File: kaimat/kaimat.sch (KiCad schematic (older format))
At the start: 4 parts

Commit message: added 2nd encoder
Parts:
- removed SW?: Rotary_Encoder, symbol Device:Rotary_Encoder
- added SW? (x2): Rotary_Encoder_Switch, symbol Device:Rotary_Encoder_Switch
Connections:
- wire segments 19 -> 43
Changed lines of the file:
@@
 EESchema Schematic File Version 4
+LIBS:kaimat-cache
 EELAYER 26 0
 EELAYER END
@@
 F 3 "" H 3300 5350 60  0000 C CNN
 	1    3300 6150
-	1    0    0    -1
-$EndComp
-$Comp
-L Device:Rotary_Encoder SW?
-U 1 1 5C4900BD
-P 2500 3450
-F 0 "SW?" H 2729 3496 50  0000 L CNN
-F 1 "Rotary_Encoder" H 2729 3405 50  0000 L CNN
-F 2 "" H 2350 3610 50  0001 C CNN
-F 3 "~" H 2500 3710 50  0001 C CNN
-	1    2500 3450
 	1    0    0    -1
 $EndComp
@@
 Wire Wire Line
 	1400 6150 2300 6150
+$Comp
+L Device:Rotary_Encoder_Switch SW?
+U 1 1 5C5B4CB3
+P 2600 4200
+F 0 "SW?" H 2600 4567 50  0000 C CNN
+F 1 "Rotary_Encoder_Switch" H 2600 4476 50  0000 C CNN
+F 2 "" H 2450 4360 50  0001 C CNN
+F 3 "~" H 2600 4460 50  0001 C CNN
+	1    2600 4200
+	1    0    0    -1
+$EndComp
 Wire Wire Line
-	650  4850 2300 4850
+	2300 4200 2100 4200
 Wire Wire Line
-	1800 3550 1800 4950
+	2100 4200 2100 4600
 Wire Wire Line
-	1800 4950 2300 4950
+	650  4850 2100 4850
+Connection ~ 2100 4850
 Wire Wire Line
-	1750 3450 1750 5050
+	2100 4850 2300 4850
 Wire Wire Line
-	1750 5050 2300 5050
+	3050 4600 3050 4300
 Wire Wire Line
-	1700 3350 1700 5150
+	3050 4300 2900 4300
 Wire Wire Line
-	1700 5150 2300 5150
+	2100 4600 3050 4600
+Connection ~ 2100 4600
 Wire Wire Line
-	1800 3550 2200 3550
+	2100 4600 2100 4850
 Wire Wire Line
-	1750 3450 2200 3450
+	2900 4100 2950 4100
 Wire Wire Line
-	1700 3350 2200 3350
+	2950 4100 2950 4700
+Wire Wire Line
+	2950 4700 2250 4700
+Wire Wire Line
+	2250 4700 2250 4950
+Wire Wire Line
+	2250 4950 2300 4950
+Wire Wire Line
+	2300 5050 2200 5050
+Wire Wire Line
+	2200 5050 2200 4300
+Wire Wire Line
+	2200 4300 2300 4300
+Wire Wire Line
+	2300 4100 2150 4100
+Wire Wire Line
+	2150 5150 2300 5150
+Wire Wire Line
+	2150 4100 2150 5150
+$Comp
+L Device:Rotary_Encoder_Switch SW?
+U 1 1 5C5B60FE
+P 2600 3500
+F 0 "SW?" H 2600 3867 50  0000 C CNN
+F 1 "Rotary_Encoder_Switch" H 2600 3776 50  0000 C CNN
+F 2 "" H 2450 3660 50  0001 C CNN
+F 3 "~" H 2600 3760 50  0001 C CNN
+	1    2600 3500
+	1    0    0    -1
+$EndComp
+Wire Wire Line
+	2100 4200 2100 3500
+Wire Wire Line
+	2100 3500 2300 3500
+Connection ~ 2100 4200
+Wire Wire Line
+	2900 3600 3050 3600
+Wire Wire Line
+	3050 3600 3050 4300
+Connection ~ 3050 4300
+Wire Wire Line
+	2900 3400 3150 3400
+Wire Wire Line
+	3150 3400 3150 3050
+Wire Wire Line
+	3150 3050 1950 3050
+Wire Wire Line
+	1950 3050 1950 6850
+Wire Wire Line
+	1950 6850 2300 6850
+Wire Wire Line
+	2300 3400 2000 3400
+Wire Wire Line
+	2000 6950 2300 6950
+Wire Wire Line
+	2000 3400 2000 6950
+Wire Wire Line
+	2300 3600 1850 3600
+Wire Wire Line
+	1850 3600 1850 7050
+Wire Wire Line
+	1850 7050 2300 7050
 $EndSCHEMATC

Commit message: added pannel
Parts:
- added D? (x2): DIODE, symbol pspice:DIODE
- added J? (x2): AudioJack2_Ground, symbol Connector:AudioJack2_Ground
- added R? (x4): R, symbol Device:R
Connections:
- new net: J?.G, R?.1 (x2)
- new net: J?.S, R?.2 (x2)
- new net: D?.1 (K), R?.1, R?.2 (x2)
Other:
- note added: "1000"
- note added: "330"
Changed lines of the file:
@@
 	650  3500 800  3500
-Wire Wire Line
-	650  4850 650  4050
-Wire Wire Line
-	650  4050 650  3500
-Connection ~ 650  4050
 Wire Wire Line
 	1400 3500 1550 3500
@@
 Wire Wire Line
 	2100 3500 2300 3500
+Wire Wire Line
+	2900 3600 3050 3600
+Wire Wire Line
+	3050 3600 3050 4300
+Wire Wire Line
+	2900 3400 3150 3400
+Wire Wire Line
+	3150 3400 3150 3050
+Wire Wire Line
+	3150 3050 1950 3050
+Wire Wire Line
+	1950 3050 1950 6850
+Wire Wire Line
+	1950 6850 2300 6850
+Wire Wire Line
+	2300 3400 2000 3400
+Wire Wire Line
+	2000 6950 2300 6950
+Wire Wire Line
+	2000 3400 2000 6950
+Wire Wire Line
+	2300 3600 1850 3600
+Wire Wire Line
+	1850 3600 1850 7050
+Wire Wire Line
+	1850 7050 2300 7050
+$Comp
+L Connector:AudioJack2_Ground J?
+U 1 1 5C5C6F4A
+P 800 900
+F 0 "J?" H 830 1225 50  0000 C CNN
+F 1 "AudioJack2_Ground" H 830 1134 50  0000 C CNN
+F 2 "" H 800 900 50  0001 C CNN
+F 3 "~" H 800 900 50  0001 C CNN
+	1    800  900
+	1    0    0    -1
+$EndComp
+$Comp
+L Device:R R?
+U 1 1 5C5C70ED
+P 1150 1100
+F 0 "R?" H 1220 1146 50  0000 L CNN
+F 1 "R" H 1220 1055 50  0000 L CNN
+F 2 "" V 1080 1100 50  0001 C CNN
+F 3 "~" H 1150 1100 50  0001 C CNN
+	1    1150 1100
+	0    -1   1    0
+$EndComp
+Text Notes 1050 1150 0    50   ~ 0
+330
+$Comp
+L Device:R R?
+U 1 1 5C5C72C2
+P 1150 800
+F 0 "R?" H 1220 846 50  0000 L CNN
+F 1 "R" H 1220 755 50  0000 L CNN
+F 2 "" V 1080 800 50  0001 C CNN
+F 3 "~" H 1150 800 50  0001 C CNN
+	1    1150 800
+	0    1    1    0
+$EndComp
+Wire Wire Line
+	800  1100 1000 1100
+Text Notes 1050 850  0    50   ~ 0
+1000
+Wire Wire Line
+	1300 800  1500 800
+Wire Wire Line
+	1300 1100 1500 1100
+Wire Wire Line
+	1500 1100 1500 800
+Wire Wire Line
+	1500 800  1700 800
+Connection ~ 1500 800
+$Comp
+L Connector:AudioJack2_Ground J?
+U 1 1 5C5D9E79
+P 800 1500
+F 0 "J?" H 830 1825 50  0000 C CNN
+F 1 "AudioJack2_Ground" H 830 1734 50  0000 C CNN
+F 2 "" H 800 1500 50  0001 C CNN
+F 3 "~" H 800 1500 50  0001 C CNN
+	1    800  1500
+	1    0    0    -1
+$EndComp
+$Comp
+L Device:R R?
+U 1 1 5C5D9E80
+P 1150 1700
+F 0 "R?" H 1220 1746 50  0000 L CNN
+F 1 "R" H 1220 1655 50  0000 L CNN
+F 2 "" V 1080 1700 50  0001 C CNN
+F 3 "~" H 1150 1700 50  0001 C CNN
+	1    1150 1700
+	0    -1   1    0
+$EndComp
+Text Notes 1050 1750 0    50   ~ 0
+330
+$Comp
+L Device:R R?
+U 1 1 5C5D9E88
+P 1150 1400
+F 0 "R?" H 1220 1446 50  0000 L CNN
+F 1 "R" H 1220 1355 50  0000 L CNN
+F 2 "" V 1080 1400 50  0001 C CNN
+F 3 "~" H 1150 1400 50  0001 C CNN
+	1    1150 1400
+	0    1    1    0
+$EndComp
+Wire Wire Line
+	800  1700 1000 1700
+Text Notes 1050 1450 0    50   ~ 0
+1000
+Wire Wire Line
+	1300 1400 1500 1400
+Wire Wire Line
+	1300 1700 1500 1700
+Wire Wire Line
+	1500 1700 1500 1400
+Wire Wire Line
+	1500 1400 1700 1400
+Connection ~ 1500 1400
+$Comp
+L pspice:DIODE D?
+U 1 1 5C5DC9CE
+P 1900 800
+F 0 "D?" H 1900 1065 50  0000 C CNN
+F 1 "DIODE" H 1900 974 50  0000 C CNN
+F 2 "" H 1900 800 50  0001 C CNN
+F 3 "~" H 1900 800 50  0001 C CNN
+	1    1900 800
+	1    0    0    -1
+$EndComp
+$Comp
+L pspice:DIODE D?
+U 1 1 5C5DCA79
+P 1900 1400
+F 0 "D?" H 1900 1665 50  0000 C CNN
+F 1 "DIODE" H 1900 1574 50  0000 C CNN
+F 2 "" H 1900 1400 50  0001 C CNN
+F 3 "~" H 1900 1400 50  0001 C CNN
+	1    1900 1400
+	1    0    0    -1
+$EndComp
+Wire Wire Line
+	650  4050 650  3500
+Wire Wire Line
+	650  4850 650  4050
+Connection ~ 650  4050
+Connection ~ 3050 4300
 Connection ~ 2100 4200
-Wire Wire Line
-	2900 3600 3050 3600
-Wire Wire Line
-	3050 3600 3050 4300
-Connection ~ 3050 4300
-Wire Wire Line
-	2900 3400 3150 3400
-Wire Wire Line
-	3150 3400 3150 3050
-Wire Wire Line
-	3150 3050 1950 3050
-Wire Wire Line
-	1950 3050 1950 6850
-Wire Wire Line
-	1950 6850 2300 6850
-Wire Wire Line
-	2300 3400 2000 3400
-Wire Wire Line
-	2000 6950 2300 6950
-Wire Wire Line
-	2000 3400 2000 6950
-Wire Wire Line
-	2300 3600 1850 3600
-Wire Wire Line
-	1850 3600 1850 7050
-Wire Wire Line
-	1850 7050 2300 7050
 $EndSCHEMATC

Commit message: schematic finished
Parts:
- removed U?: Teensy3.2, symbol teensy:Teensy3.2
- added D? (x2): DIODE, symbol pspice:DIODE
- added J? (x2): AudioJack2_Ground, symbol Connector:AudioJack2_Ground
- added R? (x4): R, symbol Device:R
- added U?: Teensy3.6, symbol teensy:Teensy3.6
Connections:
- net labels added: 3.3V, 3.3v, DACclr, DACdataout, DACldac, DACslaveSelect, DACspiclk, GND, OLEDclock, OLEDcs, OLEDdata, OLEDdc, OLEDreset, b1, b2, cvIn1, cvIn2, cvIn3, cvIn4, enc1button, enc1pinA, enc1pinB, enc2button, enc2pinA, enc2pinB, trellisSCL, trellisSDA
- wire segments 53 -> 59
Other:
- note added: "Adafruit NeoTrellis"
- note added: "TI DAC8568ICPW"
- note added: "WaveShare 128x128 OLED"
- moved on the sheet: D?, J?, R?, SW?

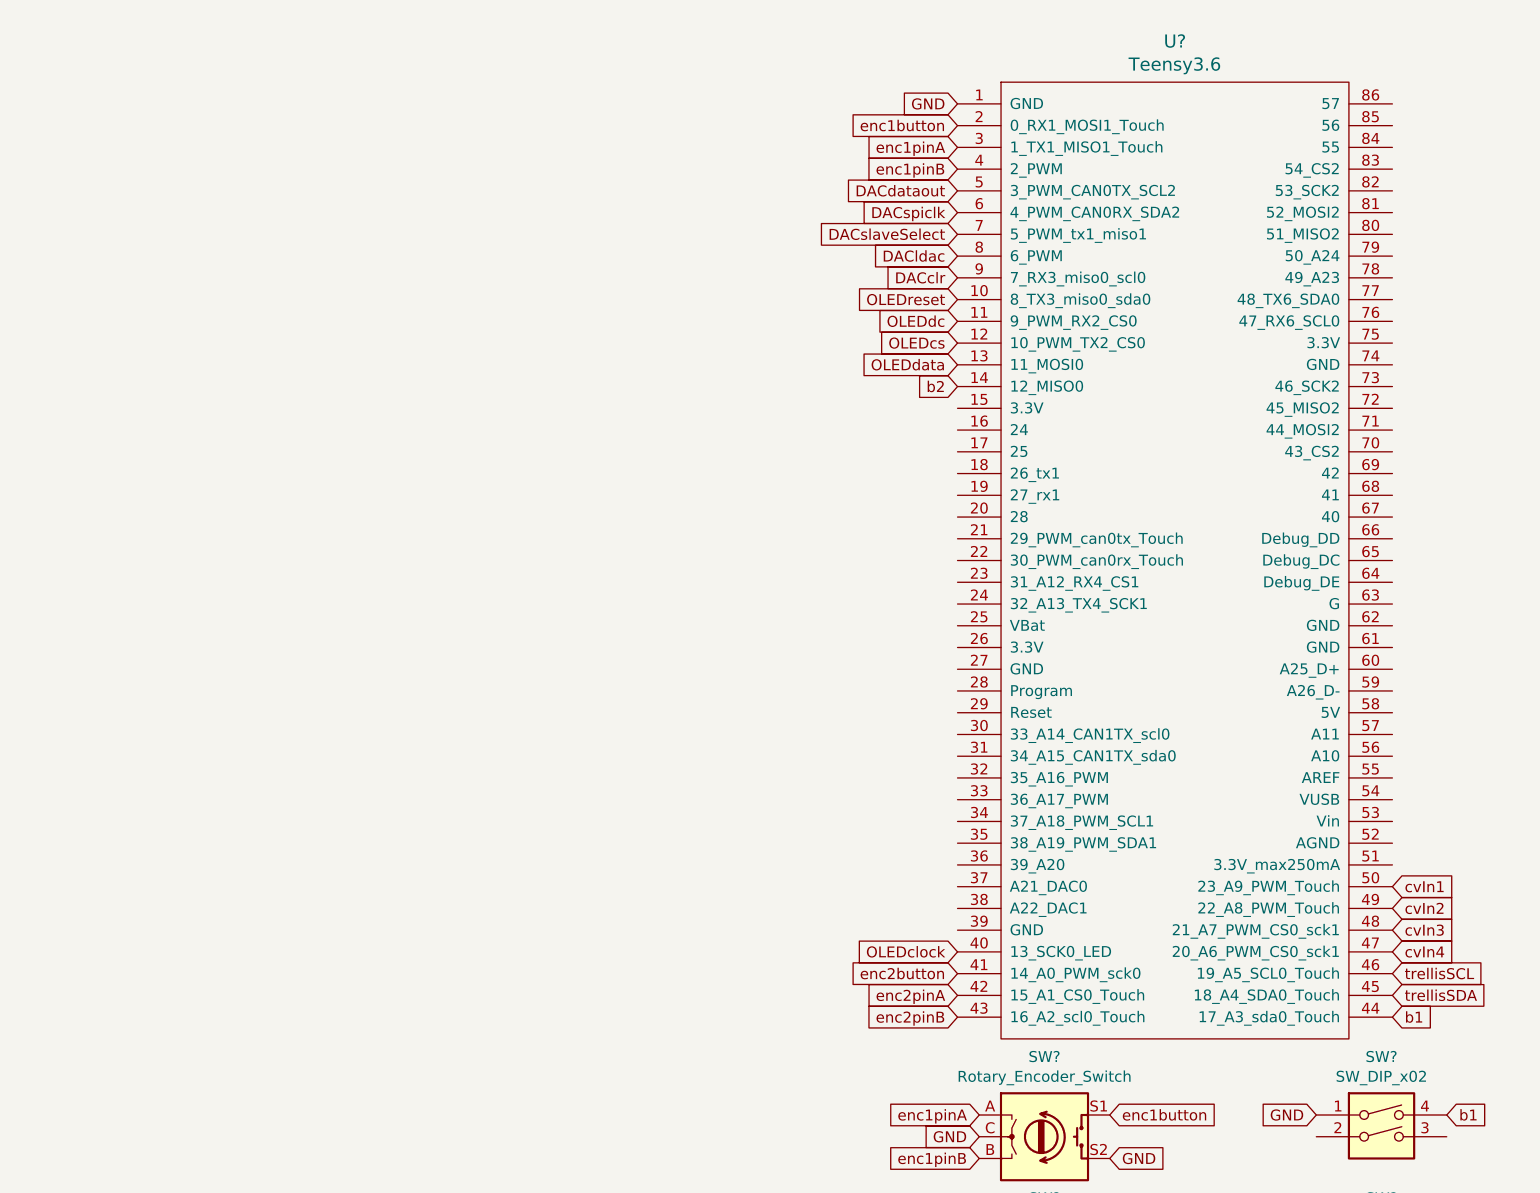
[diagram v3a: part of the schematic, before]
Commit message: schematic improved
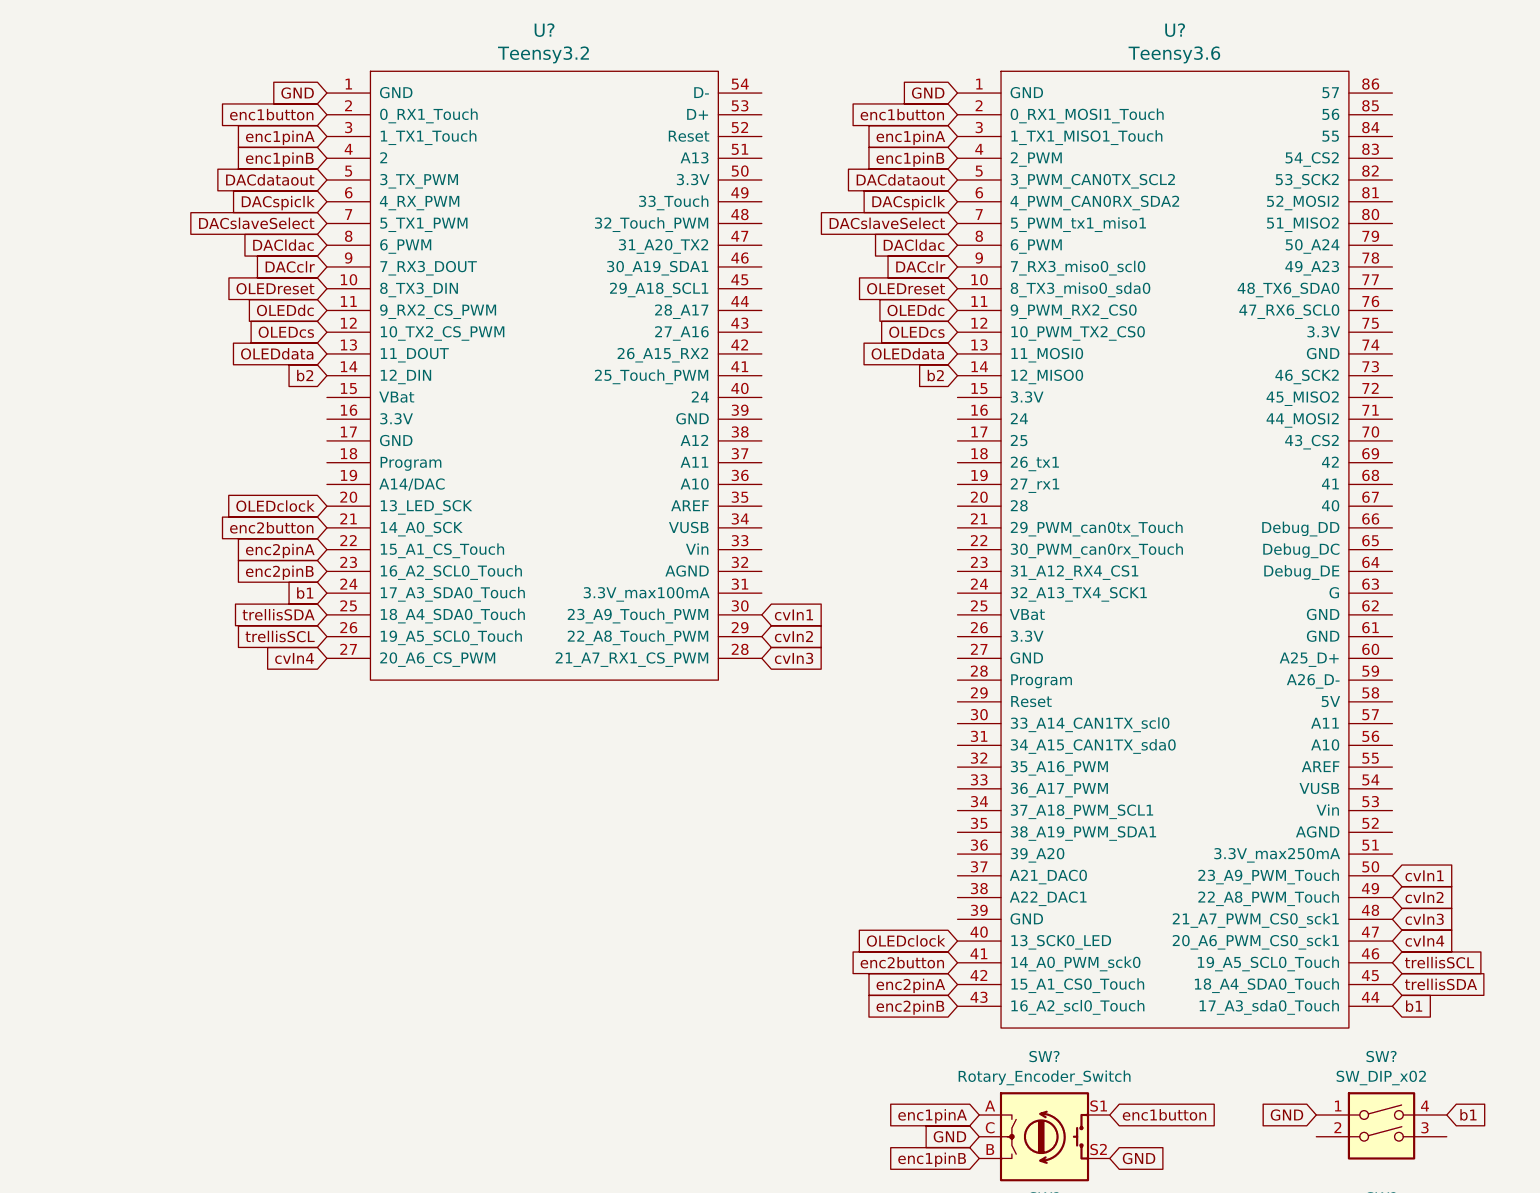
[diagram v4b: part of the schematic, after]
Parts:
- added U?: Teensy3.2, symbol teensy:Teensy3.2
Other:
- moved on the sheet: U?
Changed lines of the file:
@@
 	1    0    0    -1
 $EndComp
-Text GLabel 8750 850  0    50   Input ~ 0
+Text GLabel 8750 800  0    50   Input ~ 0
 GND
-Text GLabel 8750 950  0    50   Input ~ 0
+Text GLabel 8750 900  0    50   Input ~ 0
 enc1button
-Text GLabel 8750 1050 0    50   Input ~ 0
+Text GLabel 8750 1000 0    50   Input ~ 0
 enc1pinA
-Text GLabel 8750 1150 0    50   Input ~ 0
+Text GLabel 8750 1100 0    50   Input ~ 0
 enc1pinB
-Text GLabel 10750 5050 2    50   Input ~ 0
+Text GLabel 10750 5000 2    50   Input ~ 0
 b1
-Text GLabel 8750 2150 0    50   Input ~ 0
+Text GLabel 8750 2100 0    50   Input ~ 0
 b2
-Text GLabel 8750 4850 0    50   Input ~ 0
+Text GLabel 8750 4800 0    50   Input ~ 0
 enc2button
-Text GLabel 8750 4950 0    50   Input ~ 0
+Text GLabel 8750 4900 0    50   Input ~ 0
 enc2pinA
-Text GLabel 8750 5050 0    50   Input ~ 0
+Text GLabel 8750 5000 0    50   Input ~ 0
 enc2pinB
 Text GLabel 8850 5500 0    50   Input ~ 0
@@
 L teensy:Teensy3.6 U?
 U 1 1 5C65C83B
-P 7650 7800
-F 0 "U?" H 9750 15037 60  0000 C CNN
-F 1 "Teensy3.6" H 9750 14931 60  0000 C CNN
-F 2 "" H 9750 12650 60  0000 C CNN
-F 3 "" H 9750 12650 60  0000 C CNN
-	1    7650 7800
+P 7650 7750
+F 0 "U?" H 9750 14987 60  0000 C CNN
+F 1 "Teensy3.6" H 9750 14881 60  0000 C CNN
+F 2 "" H 9750 12600 60  0000 C CNN
+F 3 "" H 9750 12600 60  0000 C CNN
+	1    7650 7750
 	1    0    0    -1
 $EndComp
@@
 Text GLabel 2150 2750 2    50   Input ~ 0
 cvIn4
-Text GLabel 10750 4450 2    50   Input ~ 0
+Text GLabel 10750 4400 2    50   Input ~ 0
 cvIn1
-Text GLabel 10750 4550 2    50   Input ~ 0
+Text GLabel 10750 4500 2    50   Input ~ 0
 cvIn2
-Text GLabel 10750 4650 2    50   Input ~ 0
+Text GLabel 10750 4600 2    50   Input ~ 0
 cvIn3
-Text GLabel 10750 4750 2    50   Input ~ 0
+Text GLabel 10750 4700 2    50   Input ~ 0
 cvIn4
-Text GLabel 10750 4850 2    50   Input ~ 0
+Text GLabel 10750 4800 2    50   Input ~ 0
 trellisSCL
-Text GLabel 10750 4950 2    50   Input ~ 0
+Text GLabel 10750 4900 2    50   Input ~ 0
 trellisSDA
-Text GLabel 8750 1750 0    50   Input ~ 0
+Text GLabel 8750 1700 0    50   Input ~ 0
 OLEDreset
-Text GLabel 8750 1850 0    50   Input ~ 0
+Text GLabel 8750 1800 0    50   Input ~ 0
 OLEDdc
-Text GLabel 8750 1950 0    50   Input ~ 0
+Text GLabel 8750 1900 0    50   Input ~ 0
 OLEDcs
-Text GLabel 8750 2050 0    50   Input ~ 0
+Text GLabel 8750 2000 0    50   Input ~ 0
 OLEDdata
-Text GLabel 8750 4750 0    50   Input ~ 0
+Text GLabel 8750 4700 0    50   Input ~ 0
 OLEDclock
-Text GLabel 8750 1250 0    50   Input ~ 0
+Text GLabel 8750 1200 0    50   Input ~ 0
 DACdataout
-Text GLabel 8750 1350 0    50   Input ~ 0
+Text GLabel 8750 1300 0    50   Input ~ 0
 DACspiclk
-Text GLabel 8750 1450 0    50   Input ~ 0
+Text GLabel 8750 1400 0    50   Input ~ 0
 DACslaveSelect
-Text GLabel 8750 1550 0    50   Input ~ 0
+Text GLabel 8750 1500 0    50   Input ~ 0
 DACldac
-Text GLabel 8750 1650 0    50   Input ~ 0
+Text GLabel 8750 1600 0    50   Input ~ 0
 DACclr
 $Bitmap
@@
 Data
 89 50 4E 47 0D 0A 1A 0A 00 00 00 0D 49 48 44 52 00 00 01 CB 00 00 01 85 08 02 00 00 00 1D 32 4F
-0C 00 00 00 03 73 42 49 54 08 08 08 DB E1 4F E0 00 00 00 09 70 48 59 73 00 00 0E C3 00 00 0E C3
-01 C7 6F A8 64 00 00 20 00 49 44 41 54 78 9C EC 5D 67 B8 1D 55 D5 7E D7 DA 7B E6 9C 7B 13 52 E9
+0C 00 00 00 03 73 42 49 54 08 08 08 DB E1 4F E0 00 00 00 09 70 48 59 73 00 00 0E 74 00 00 0E 74
+01 6B 24 B3 D6 00 00 20 00 49 44 41 54 78 9C EC 5D 67 B8 1D 55 D5 7E D7 DA 7B E6 9C 7B 13 52 E9
 81 40 02 81 A0 F4 22 4A 47 29 16 44 69 09 06 10 91 A6 7C 80 20 55 14 2C A0 22 22 5D 4A 28 89 B4
 50 42 15 14 15 05 05 91 4E E8 35 01 42 07 43 48 BB F7 9C 99 BD D7 FA 7E EC 99 39 73 6E 6E 1A 49
@@
 Text Notes 2050 3300 2    50   ~ 0
 TI DAC8568ICPW
+$Comp
+L teensy:Teensy3.2 U?
+U 1 1 5C6D43F0
+P 6850 2100
+F 0 "U?" H 6850 3687 60  0000 C CNN
+F 1 "Teensy3.2" H 6850 3581 60  0000 C CNN
+F 2 "" H 6850 1300 60  0000 C CNN
+F 3 "" H 6850 1300 60  0000 C CNN
+	1    6850 2100
+	1    0    0    -1
+$EndComp
+Text GLabel 5850 800  0    50   Input ~ 0
+GND
+Text GLabel 5850 900  0    50   Input ~ 0
+enc1button
+Text GLabel 5850 1000 0    50   Input ~ 0
+enc1pinA
+Text GLabel 5850 1100 0    50   Input ~ 0
+enc1pinB
+Text GLabel 5850 2100 0    50   Input ~ 0
+b2
+Text GLabel 5850 1700 0    50   Input ~ 0
+OLEDreset
+Text GLabel 5850 1800 0    50   Input ~ 0
+OLEDdc
+Text GLabel 5850 1900 0    50   Input ~ 0
+OLEDcs
+Text GLabel 5850 2000 0    50   Input ~ 0
+OLEDdata
+Text GLabel 5850 1200 0    50   Input ~ 0
+DACdataout
+Text GLabel 5850 1300 0    50   Input ~ 0
+DACspiclk
+Text GLabel 5850 1400 0    50   Input ~ 0
+DACslaveSelect
+Text GLabel 5850 1500 0    50   Input ~ 0
+DACldac
+Text GLabel 5850 1600 0    50   Input ~ 0
+DACclr
+Text GLabel 5850 2800 0    50   Input ~ 0
+enc2button
+Text GLabel 5850 2900 0    50   Input ~ 0
+enc2pinA
+Text GLabel 5850 3000 0    50   Input ~ 0
+enc2pinB
+Text GLabel 5850 2700 0    50   Input ~ 0
+OLEDclock
+Text GLabel 5850 3100 0    50   Input ~ 0
+b1
+Text GLabel 5850 3200 0    50   Input ~ 0
+trellisSDA
+Text GLabel 5850 3300 0    50   Input ~ 0
+trellisSCL
+Text GLabel 5850 3400 0    50   Input ~ 0
+cvIn4
+Text GLabel 7850 3200 2    50   Input ~ 0
+cvIn1
+Text GLabel 7850 3300 2    50   Input ~ 0
+cvIn2
+Text GLabel 7850 3400 2    50   Input ~ 0
+cvIn3
 $EndSCHEMATC

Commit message: improved schematic
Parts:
- removed U?: Teensy3.6, symbol teensy:Teensy3.6
- removed U?: Teensy3.2, symbol teensy:Teensy3.2
- added DAC1: TI_DAC8568_ICPW, symbol KaimatKicadLib:TI_DAC8568_ICPW
- added MCU1: Teensy3.2, symbol KaimatKicadLib:Teensy3.2
- added MCU2: Teensy3.6, symbol KaimatKicadLib:Teensy3.6
- added U1: Waveshare_128x128_OLED_SSD1327, symbol KaimatKicadLib:Waveshare_128x128_OLED_SSD1327
- added U2: Adafruit_NeoTrellis, symbol KaimatKicadLib:Adafruit_NeoTrellis
- gave numbers to parts that had none: 20
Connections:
- wire segments 59 -> 20
- no-connect marks 0 -> 6
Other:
- note removed: "Adafruit NeoTrellis"
- note removed: "TI DAC8568ICPW"
- note removed: "WaveShare 128x128 OLED"
- moved on the sheet: SW1, SW2, SW4
